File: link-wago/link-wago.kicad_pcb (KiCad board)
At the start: 4 copper layers, 72 x 29 mm, 37 parts, among them J101 2x05_Horizontal, J102 NE8FAH, J103 DX07S016JA3, J104 2x05_Horizontal, J105 NE8FAH, J106 WAGO 2601-1101, J107 WAGO 2065-100, J108 WAGO 2065-100, J109 WAGO 2601-1101, J110 WAGO 2065-100, J111 WAGO 2065-100, U501 TPSM33625

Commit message: Use date as revision
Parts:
- U501: footprint V2_Converter_DCDC:TPSM33625 -> V2_Converter_DCDC:QFN-11
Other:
- board text added: "Next: Move WAGO further in"
- board text removed: "Move WAGOs further in"

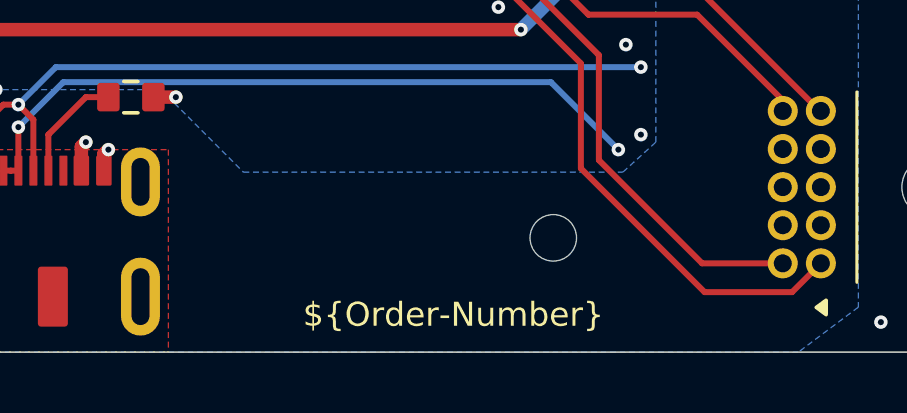
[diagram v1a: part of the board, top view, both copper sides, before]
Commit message: Replace Order_Number
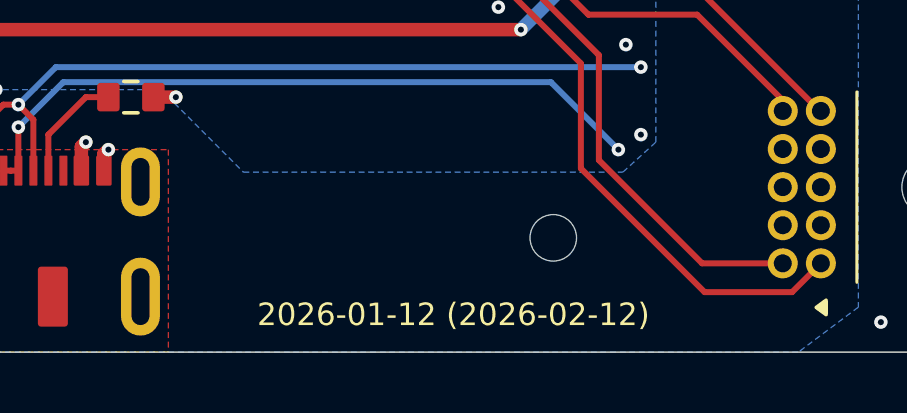
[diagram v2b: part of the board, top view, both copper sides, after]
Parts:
- INFO102: value Order_Number -> ~; footprint V2_Production:Order_Number -> V2_Production:Revision
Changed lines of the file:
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@@
 	(paper "A4")
 	(title_block
-		(date "2026-02-10")
+		(date "2026-02-12")
 		(rev "2026-01-12")
 	)
@@
 		)
 	)
-	(property "Order-Number" "JLCJLCJLCJLC")
 	(net 0 "")
 	(net 1 "GND")
@@
 			)
 		)
-		(property "Description" ""
+		(property "Description" "Resistor, small symbol"
 			(at 0 0 0)
 			(layer "F.Fab")
@@
 			)
 		)
-		(property "Description" ""
+		(property "Description" "Fiducial Marker"
 			(at 0 0 0)
 			(unlocked yes)
@@
 			)
 		)
-		(property "Description" ""
+		(property "Description" "Fiducial Marker"
 			(at 0 0 0)
 			(unlocked yes)
@@
 		(embedded_fonts no)
 	)
-	(footprint "V2_Production:Order_Number"
+	(footprint "V2_Production:Revision"
 		(layer "F.Cu")
 		(at 166.75 113.75)
@@
 			)
 		)
-		(property "Value" "Order_Number"
+		(property "Value" "~"
 			(at 0 2.27 0)
 			(unlocked yes)
@@
 		(sheetname "/")
 		(sheetfile "link-wago.kicad_sch")
-		(attr exclude_from_pos_files exclude_from_bom)
-		(fp_rect
-			(start -7 -0.75)
-			(end 7 0.75)
-			(stroke
-				(width 0.05)
-				(type default)
+		(attr exclude_from_pos_files exclude_from_bom allow_missing_courtyard)
+		(fp_text user "${REVISION} (${ISSUE_DATE})"
+			(at 0 0 0)
+			(unlocked yes)
+			(layer "F.SilkS")
+			(effects
+				(font
+					(size 0.75 0.75)
+					(thickness 0.1)
+				)
 			)
-			(fill no)
-			(layer "F.CrtYd")
 		)
-		(fp_text user "${Order-Number}"
+		(fp_text user "${REVISION} (${ISSUE_DATE})"
 			(at 0 0 0)
 			(unlocked yes)
-			(layer "F.SilkS")
+			(layer "F.Fab")
 			(effects
 				(font
-					(size 0.8 0.8)
-					(thickness 0.12)
+					(size 0.75 0.75)
+					(thickness 0.1)
 				)
 			)
@@
 			)
 		)
-		(property "Description" ""
+		(property "Description" "Amphenol – Minitek127"
 			(at 0 0 270)
 			(unlocked yes)
@@
 			)
 		)
-		(property "Description" ""
+		(property "Description" "Transient Voltage Suppressor Diode, Bidirectional, 36.7-40.6V"
 			(at 0 0 90)
 			(unlocked yes)
@@
 			)
 		)
-		(property "Description" ""
+		(property "Description" "Resistor, small symbol"
 			(at 0 0 0)
 			(layer "F.Fab")
@@
 			)
 		)
-		(property "Description" ""
+		(property "Description" "Unpolarized capacitor, small symbol"
 			(at 0 0 90)
 			(layer "F.Fab")
@@
 			)
 		)
-		(property "Description" ""
+		(property "Description" "Unpolarized capacitor, small symbol"
 			(at 0 0 270)
 			(layer "F.Fab")
@@
 			)
 		)
-		(property "Description" ""
+		(property "Description" "Resistor, small symbol"
 			(at 0 0 180)
 			(layer "F.Fab")
@@
 			)
 		)
-		(property "Description" ""
+		(property "Description" "Amphenol – Minitek127"
 			(at 0 0 90)
 			(unlocked yes)
@@
 			)
 		)
-		(property "Description" ""
+		(property "Description" "Unpolarized capacitor, small symbol"
 			(at 0 0 270)
 			(layer "F.Fab")
@@
 			)
 		)
-		(property "Description" ""
+		(property "Description" "Unpolarized capacitor, small symbol"
 			(at 0 0 270)
 			(layer "F.Fab")
@@
 			)
 		)
-		(property "Description" ""
+		(property "Description" "Unpolarized capacitor, small symbol"
 			(at 0 0 90)
 			(layer "F.Fab")
@@
 			)
 		)
-		(property "Description" ""
+		(property "Description" "Resistor, small symbol"
 			(at 0 0 0)
 			(layer "F.Fab")
@@
 			)
 		)
-		(property "Description" ""
+		(property "Description" "Fiducial Marker"
 			(at 0 0 0)
 			(unlocked yes)
@@
 			)
 		)
-		(property "Description" ""
+		(property "Description" "Unpolarized capacitor, small symbol"
 			(at 0 0 90)
 			(layer "F.Fab")

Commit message: Export stencil
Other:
- board text removed: "Next: Move WAGO further in"
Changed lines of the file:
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@@
 	(paper "A4")
 	(title_block
-		(date "2026-02-12")
+		(date "2026-02-25")
 		(rev "2026-01-12")
 	)
@@
 			)
 		)
-		(property "Description" "Resistor, small symbol"
+		(property "Description" ""
 			(at 0 0 0)
 			(layer "F.Fab")
@@
 			)
 		)
-		(property "Description" "Fiducial Marker"
+		(property "Description" ""
 			(at 0 0 0)
 			(unlocked yes)
@@
 			)
 		)
-		(property "Description" "Fiducial Marker"
+		(property "Description" ""
 			(at 0 0 0)
 			(unlocked yes)
@@
 			)
 		)
-		(property "Sim.Enable" "0"
-			(at 0 0 0)
-			(unlocked yes)
-			(layer "F.Fab")
-			(hide yes)
-			(effects
-				(font
-					(size 1 1)
-					(thickness 0.15)
-				)
-			)
-		)
 		(sheetname "/")
 		(sheetfile "link-wago.kicad_sch")
@@
 			)
 		)
-		(property "Description" "Amphenol – Minitek127"
+		(property "Description" ""
 			(at 0 0 270)
 			(unlocked yes)
@@
 			)
 		)
-		(property "Description" "Transient Voltage Suppressor Diode, Bidirectional, 36.7-40.6V"
+		(property "Description" ""
 			(at 0 0 90)
 			(unlocked yes)
@@
 			)
 		)
-		(property "Description" "Resistor, small symbol"
+		(property "Description" ""
 			(at 0 0 0)
 			(layer "F.Fab")
@@
 			)
 		)
-		(property "Description" "Unpolarized capacitor, small symbol"
+		(property "Description" ""
 			(at 0 0 90)
 			(layer "F.Fab")
@@
 			)
 		)
-		(property "Description" "Unpolarized capacitor, small symbol"
+		(property "Description" ""
 			(at 0 0 270)
 			(layer "F.Fab")
@@
 			)
 		)
-		(property "Description" "Resistor, small symbol"
+		(property "Description" ""
 			(at 0 0 180)
 			(layer "F.Fab")
@@
 			)
 		)
-		(property "Description" "Amphenol – Minitek127"
+		(property "Description" ""
 			(at 0 0 90)
 			(unlocked yes)
@@
 			)
 		)
-		(property "Description" "Unpolarized capacitor, small symbol"
+		(property "Description" ""
 			(at 0 0 270)
 			(layer "F.Fab")
@@
 			)
 		)
-		(property "Description" "Unpolarized capacitor, small symbol"
+		(property "Description" ""
 			(at 0 0 270)
 			(layer "F.Fab")
@@
 			)
 		)
-		(property "Description" "Unpolarized capacitor, small symbol"
+		(property "Description" ""
 			(at 0 0 90)
 			(layer "F.Fab")
@@
 			)
 		)
-		(property "Description" "Resistor, small symbol"
+		(property "Description" ""
 			(at 0 0 0)
 			(layer "F.Fab")
@@
 			)
 		)
-		(property "Description" "Fiducial Marker"
+		(property "Description" ""
 			(at 0 0 0)
 			(unlocked yes)
@@
 			)
 		)
-		(property "Description" "Unpolarized capacitor, small symbol"
+		(property "Description" ""
 			(at 0 0 90)
 			(layer "F.Fab")
@@
 		(layer "Edge.Cuts")
 	)
-	(gr_text "Next: Move WAGO further in"
-		(at 116 77.5 0)
-		(layer "F.Fab")
-		(effects
-			(font
-				(size 1.27 1.27)
-			)
-			(justify left)
-		)
-	)
 	(segment

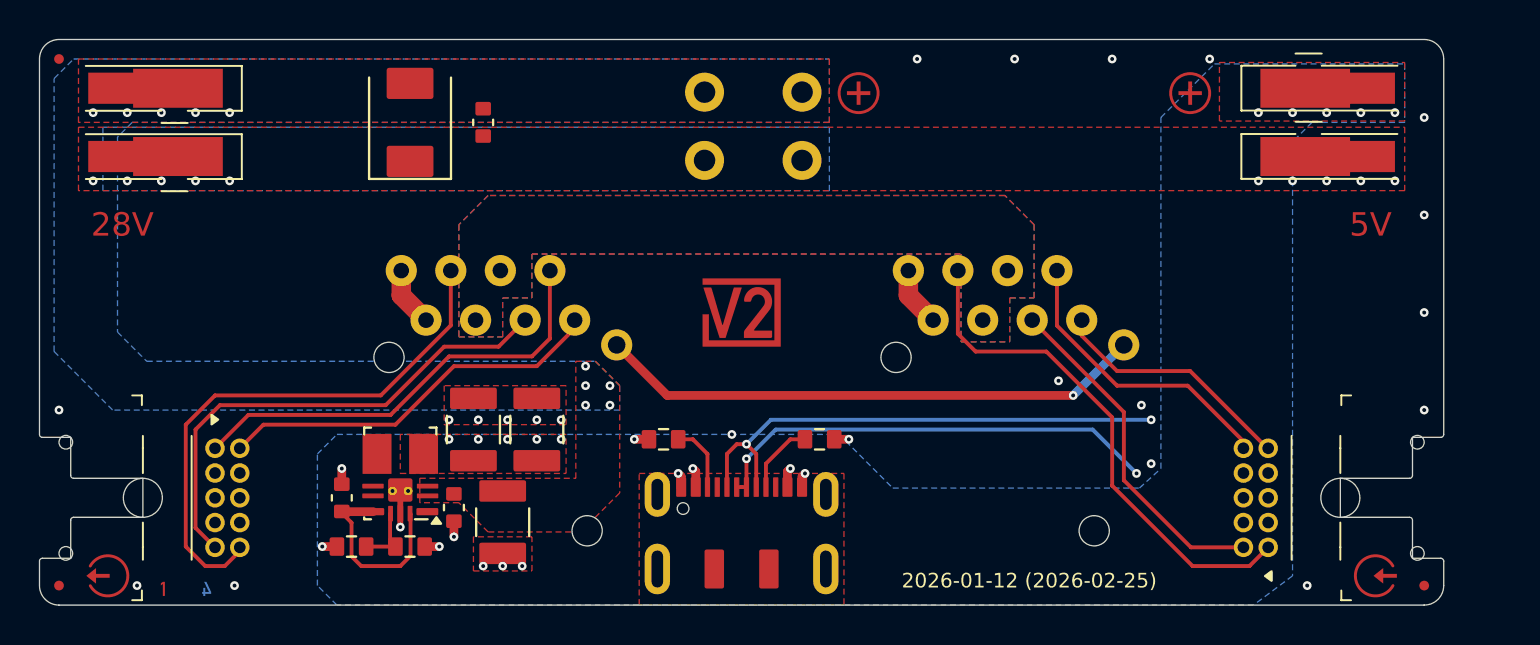
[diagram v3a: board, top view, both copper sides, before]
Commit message: Replace step-down
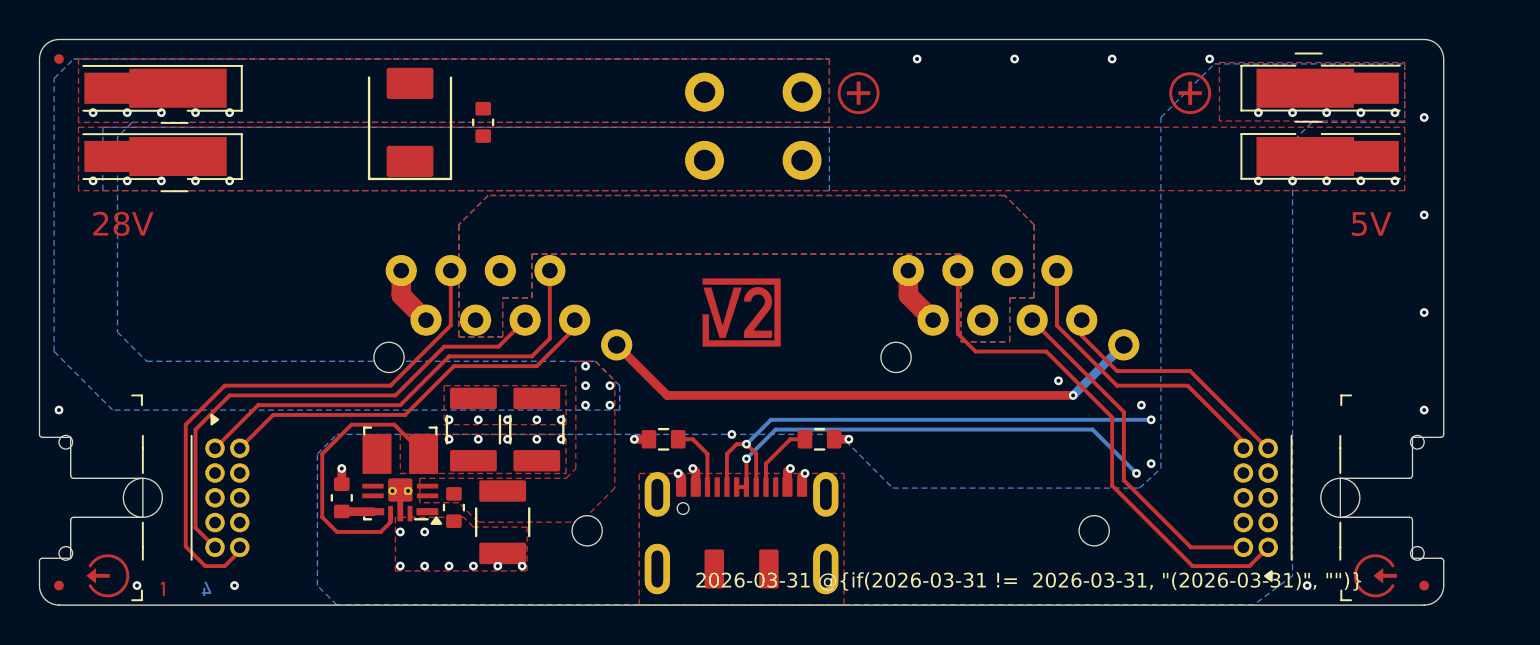
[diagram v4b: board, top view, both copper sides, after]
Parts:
- removed R501: 40k2, V2_Resistor_SMD:R_0603
- removed R502: 10k, V2_Resistor_SMD:R_0603
- U501: value TPSM33625 -> TPSM33620S5QRDNRQ1
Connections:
- net +VBUS renamed /+VBUS
- net +VLINK renamed /+VLINK
- net Shield renamed /Shield
- U501 pad 11: /Power +5V/Vcc -> GND
- U501 pad 9: /Power +5V/Feedback -> +5V
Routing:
- net +5V: track 0.68 -> 14.2 mm, vias 11 -> 10
- net /Power +5V/Vcc: track 9.70 -> 1.64 mm
- net /Power +5V/Feedback: track 3.13 -> 0.00 mm
- net GND: track 12.1 -> 9.77 mm, vias 42 -> 44

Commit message: Update
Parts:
- renumbered C505 to C503, C503 to C504, C504 to C505, ICON102 to ICON101, ICON101 to ICON102, ICON106 to ICON105, ICON105 to ICON106, J106 to J101, J109 to J102, J102 to J103, J105 to J104, J101 to J105, J104 to J106, J110 to J108, J108 to J109, J111 to J110, J103 to J111

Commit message: Refresh
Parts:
- C101, C502, C503: footprint V2_Capacitor_SMD:C_0603 -> V2_Capacitor_SMD:C_1608
- C501, C504, C505: footprint V2_Capacitor_SMD:C_1210 -> V2_Capacitor_SMD:C_3225
- INFO101: value Layer_Numbers -> Layer_Numbers-4; footprint V2_Production:Layer_Numbers -> V2_Production:Layer_Numbers-4
- R101, R102: footprint V2_Resistor_SMD:R_0603 -> V2_Resistor_SMD:R_1608
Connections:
- J111 pad V: /+VBUS -> unconnected-(J111-VBUS-PadV)
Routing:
- net /+VBUS: track 7.85 -> 0.00 mm, vias 2 -> 0
- net /USB-: track 37.4 -> 39.5 mm, vias 2 -> 0
- net /USB+: track 29.5 -> 30.7 mm, vias 2 -> 1
- net /Plug-RX-A: track 17.7 -> 16.7 mm
- net /Plug-RX-B: track 26.5 -> 25.9 mm
- net GND: vias 44 -> 42
